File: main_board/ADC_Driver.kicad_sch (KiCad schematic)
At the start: 16 parts, among them U5 LMH6550MA, U6 LMV321IDBVR

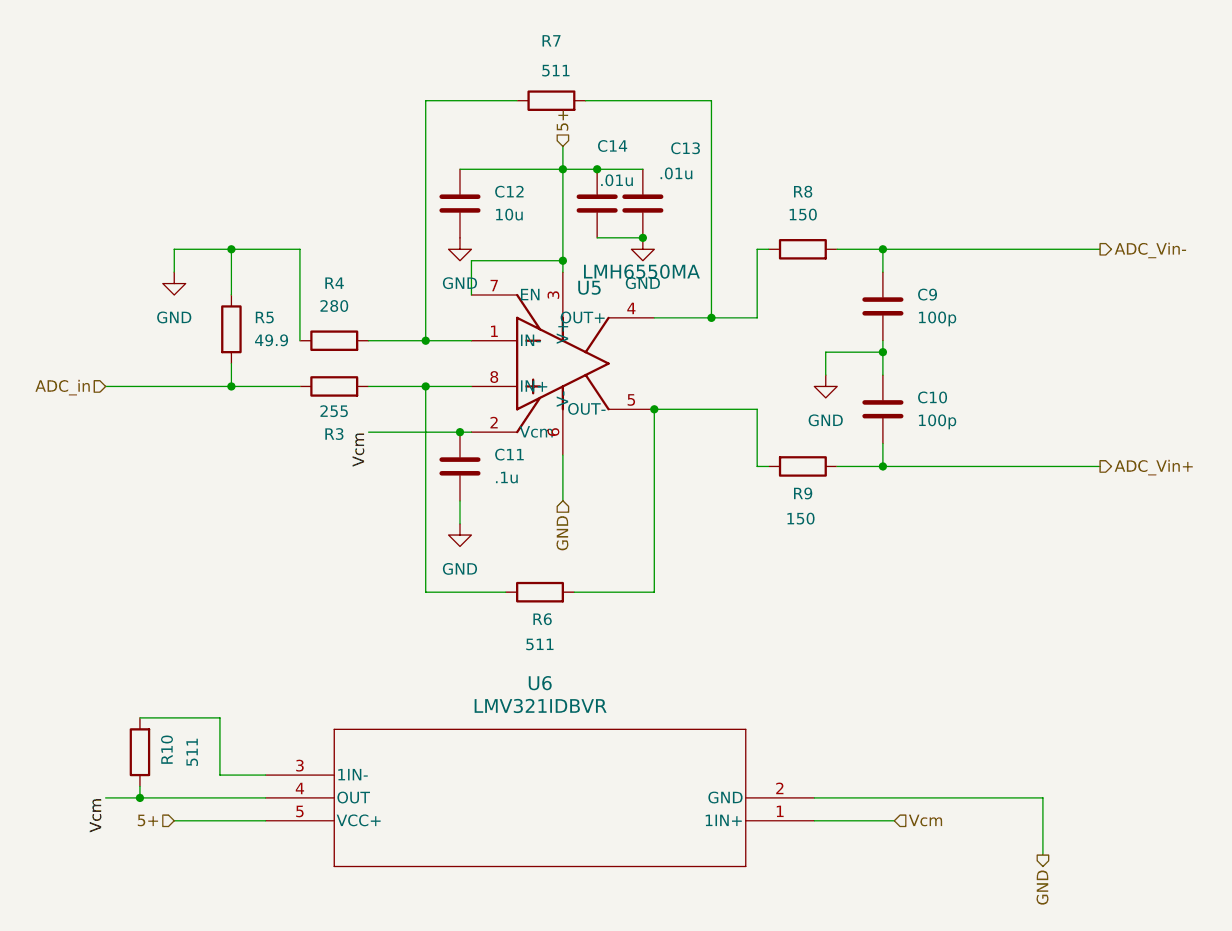
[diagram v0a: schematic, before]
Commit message: remove hierarchical gnd and +5v pins in favor of using global for all power
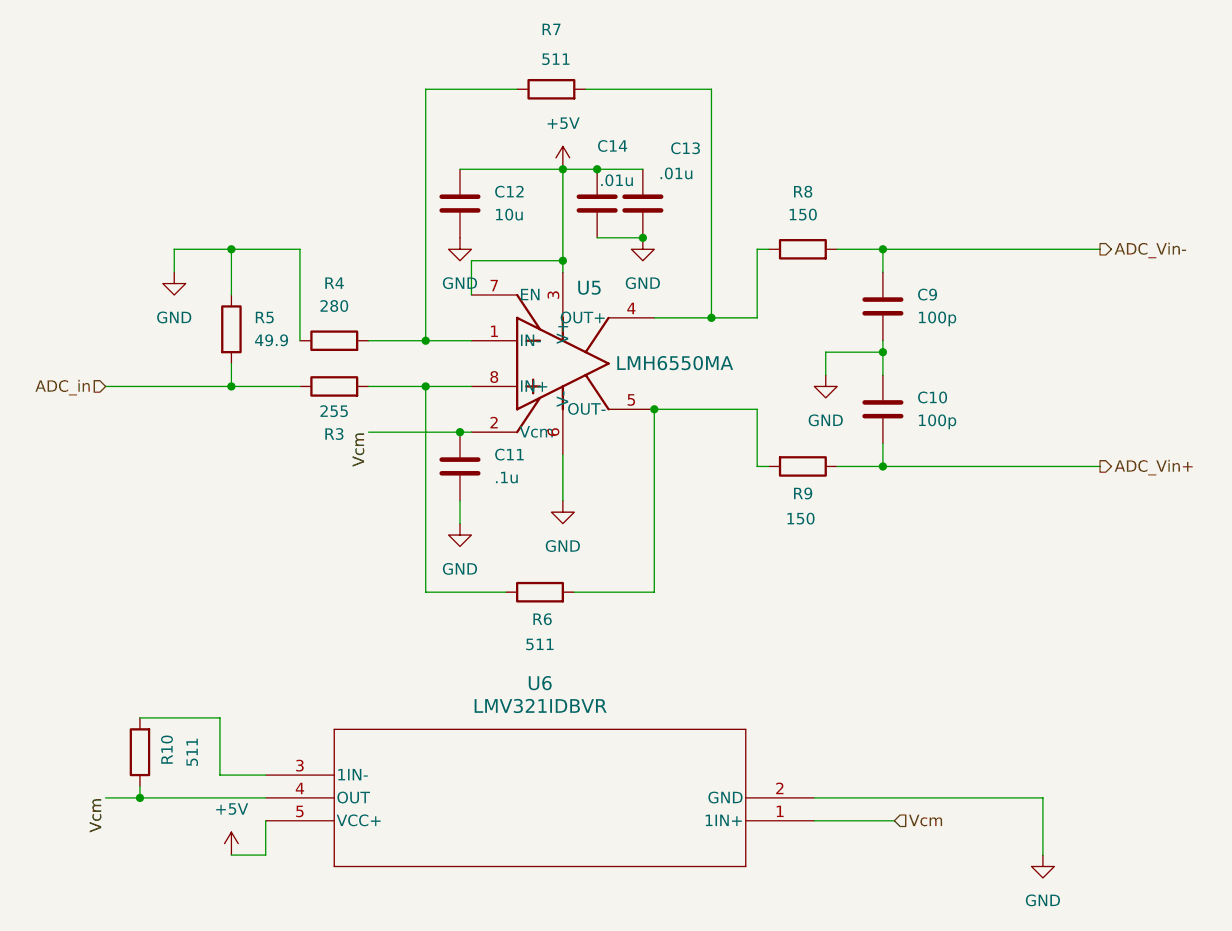
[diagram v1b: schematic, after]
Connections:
- net 5+ renamed +5V
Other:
- moved on the sheet: R7
